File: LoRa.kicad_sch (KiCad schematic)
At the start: 0 parts

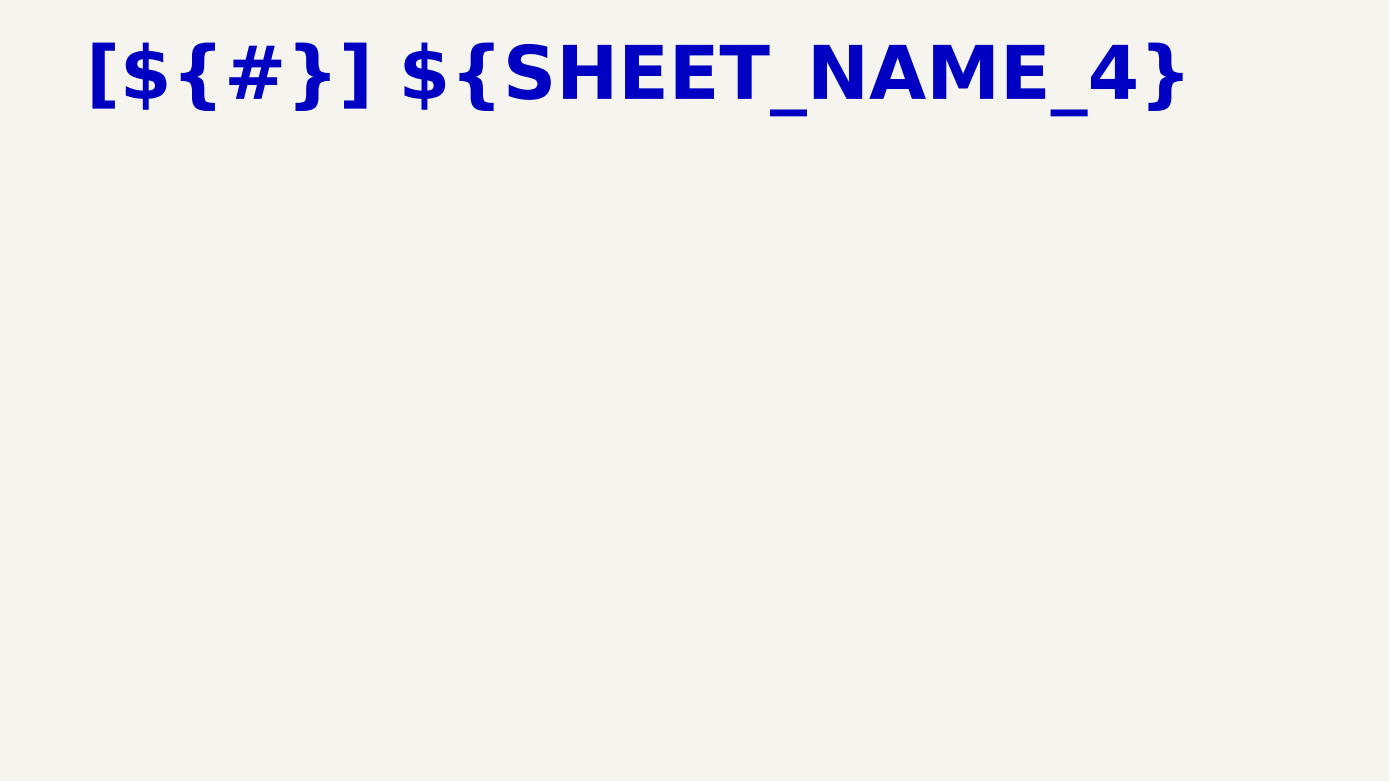
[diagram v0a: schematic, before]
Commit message: Pasted schematics from previous design
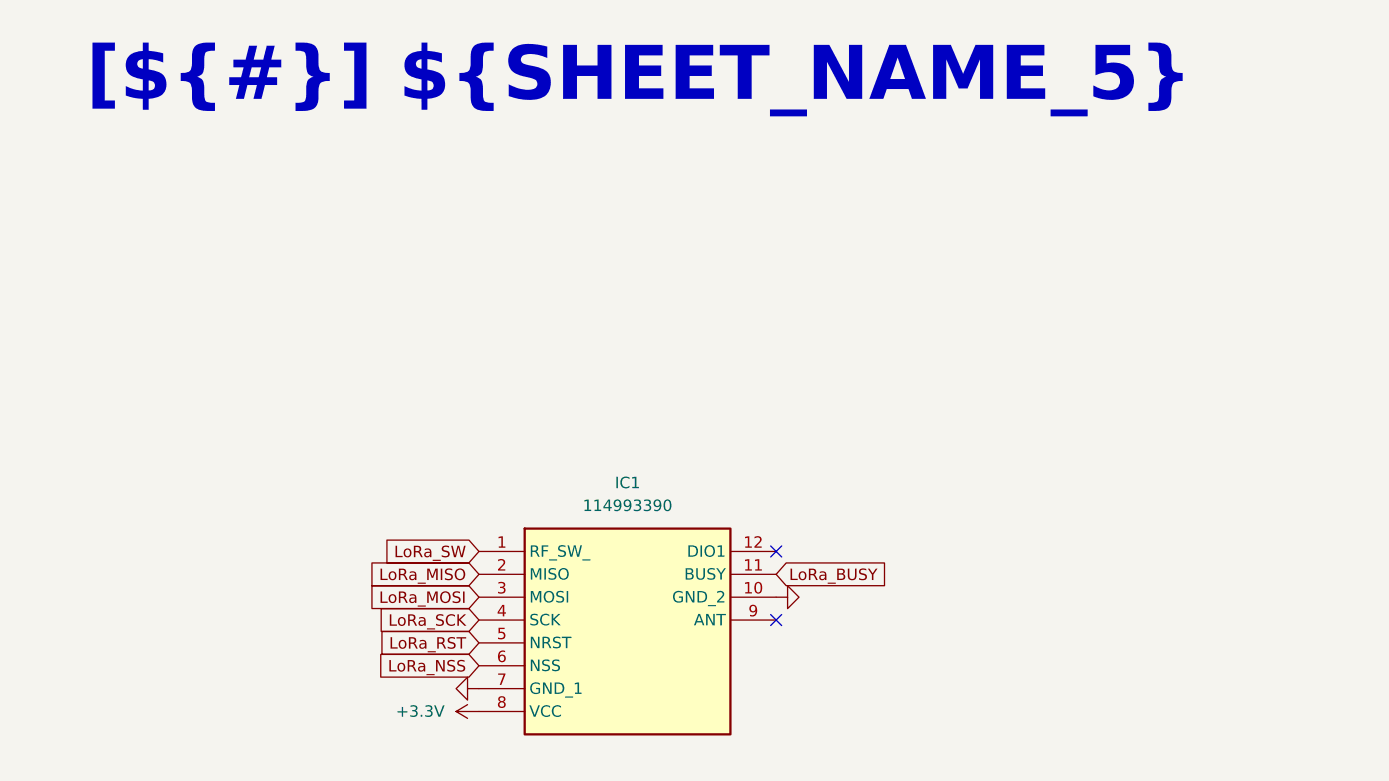
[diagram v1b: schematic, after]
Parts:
- added IC1: 114993390, Project_Components:114993390, symbol Project_Components:114993390
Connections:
- new net +3.3V: IC1.8 (VCC)
- new net GND: IC1.10 (GND_2), IC1.7 (GND_1)
- new net LoRa_BUSY: IC1.11 (BUSY)
- new net LoRa_MISO: IC1.2 (MISO)
- new net LoRa_MOSI: IC1.3 (MOSI)
- new net LoRa_NSS: IC1.6 (NSS)
- new net LoRa_RST: IC1.5 (NRST)
- new net LoRa_SCK: IC1.4 (SCK)
- new net LoRa_SW: IC1.1 (RF_SW_)
- no-connect marks 0 -> 2

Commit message: Finished preliminary project schematics and architecture
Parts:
- IC1: footprint Project_Components:114993390 -> 00_lora:wio-sx1262

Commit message: Minor schematic adjustments
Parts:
- IC1: footprint 00_lora:wio-sx1262 -> Project_Components:114993390
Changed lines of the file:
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@@
 			)
 		)
-		(property "Footprint" "00_lora:wio-sx1262"
+		(property "Footprint" "Project_Components:114993390"
 			(at 130.81 78.74 0)
 			(hide yes)

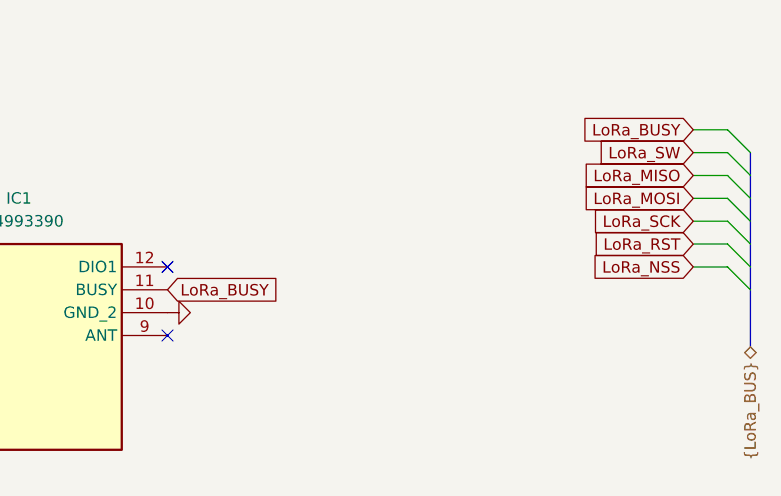
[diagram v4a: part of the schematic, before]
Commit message: Connected DIO1 of lora module
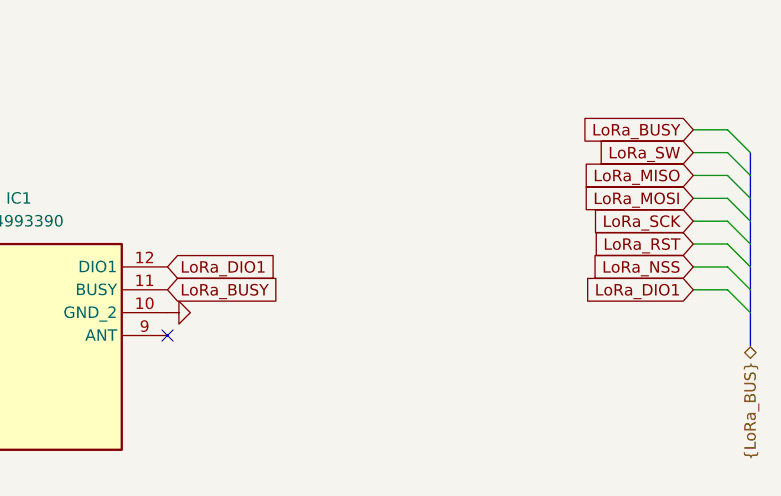
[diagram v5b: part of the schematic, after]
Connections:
- net LoRa_DIO1: now reaches IC1.12 (DIO1)
- no-connect marks 2 -> 1
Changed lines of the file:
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@@
 		(at 163.83 86.36)
 	)
-	(no_connect
-		(at 163.83 78.74)
-	)
 	(bus_entry
 		(at 226.06 78.74)
@@
 	)
 	(bus_entry
+		(at 226.06 81.28)
+		(size 2.54 2.54)
+		(stroke
+			(width 0)
+			(type default)
+		)
+	)
+	(bus_entry
 		(at 226.06 73.66)
 		(size 2.54 2.54)
@@
 	(wire
 		(pts
+			(xy 222.25 81.28) (xy 226.06 81.28)
+		)
+		(stroke
+			(width 0)
+			(type default)
+		)
+	)
+	(wire
+		(pts
 			(xy 222.25 76.2) (xy 226.06 76.2)
 		)
@@
 		)
 	)
+	(global_label "LoRa_DIO1"
+		(shape input)
+		(at 163.83 78.74 0)
+		(fields_autoplaced yes)
+		(effects
+			(font
+				(size 1.27 1.27)
+			)
+			(justify left)
+		)
+		(property "Intersheetrefs" "${INTERSHEET_REFS}"
+			(at 176.7937 78.74 0)
+			(hide yes)
+			(show_name no)
+			(do_not_autoplace no)
+			(effects
+				(font
+					(size 1.27 1.27)
+				)
+				(justify left)
+			)
+		)
+	)
 	(global_label "LoRa_MOSI"
 		(shape input)
@@
 			)
 		)
+	)
+	(global_label "LoRa_DIO1"
+		(shape input)
+		(at 222.25 81.28 180)
+		(fields_autoplaced yes)
+		(effects
+			(font
+				(size 1.27 1.27)
+			)
+			(justify right)
+		)
+		(property "Intersheetrefs" "${INTERSHEET_REFS}"
+			(at 209.2863 81.28 0)
+			(hide yes)
+			(show_name no)
+			(do_not_autoplace no)
+			(effects
+				(font
+					(size 1.27 1.27)
+				)
+				(justify right)
+			)
+		)
